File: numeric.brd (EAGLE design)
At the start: 94.9 x 61.6 mm, 28 parts, among them IC1 MEGA8-AI, Q2 BC817-16SMD, Q3 BC817-16SMD, SW2 EC12E_SW

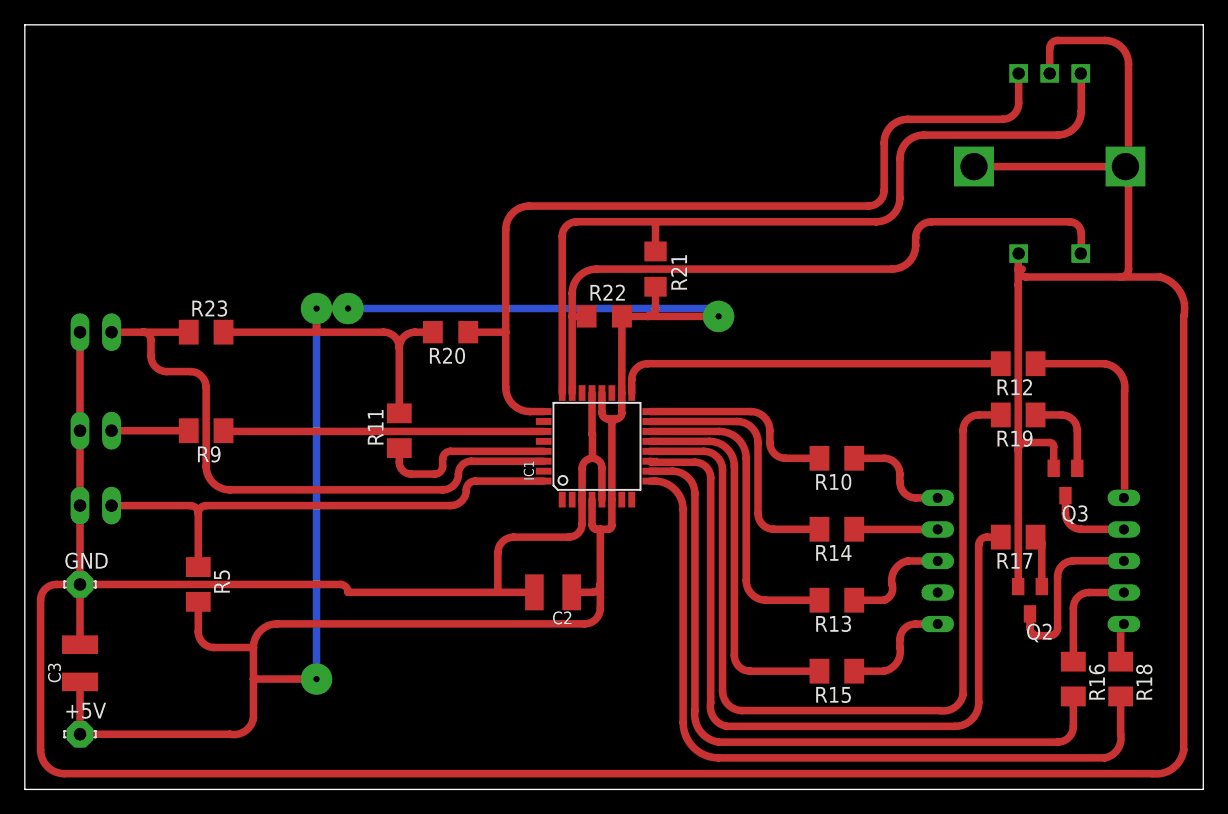
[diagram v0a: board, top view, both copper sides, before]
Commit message: Добавил разводку на горизонтальную плату
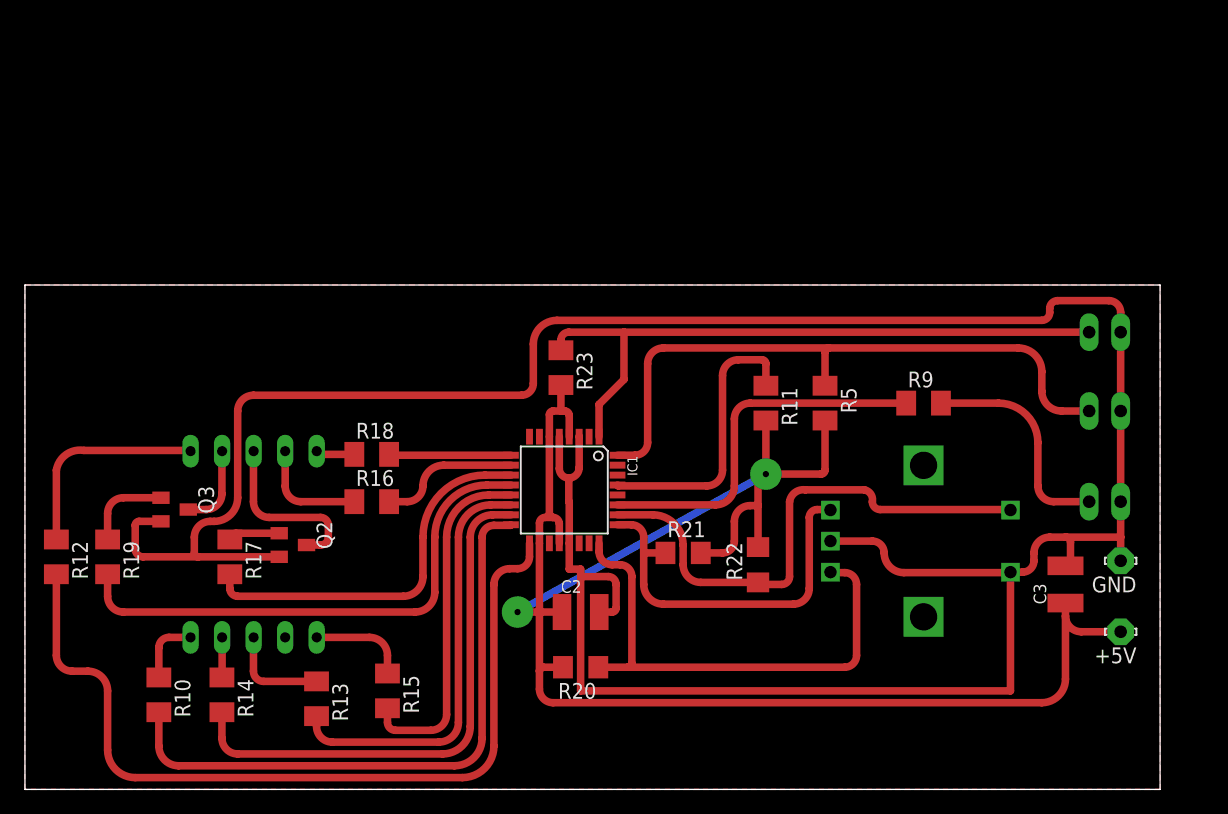
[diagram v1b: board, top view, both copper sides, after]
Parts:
- moved +5V 84.2 mm to (88.3, 12.7), turned to 180 degrees
- moved GND 83.8 mm to (88.3, 18.4), turned to 180 degrees
- moved TO_4N33 81.6 mm to (87.0, 30.5), turned to 0 degrees
- moved TO_MOC3061 81.5 mm to (87.0, 23.2), turned to 0 degrees
- moved BUTTON 81.3 mm to (87.0, 36.8), turned to 180 degrees
- moved C3 79.6 mm to (83.8, 16.5)
- moved R12 79.0 mm to (2.54, 18.7), turned to 270 degrees
- moved R19 74.2 mm to (6.67, 18.7), turned to 270 degrees
- moved Q3 71.8 mm to (12.1, 22.5), turned to 270 degrees
- moved DIS1 69.5 mm to (11.4, 19.4), turned to 0 degrees
- moved R17 63.5 mm to (16.5, 18.7), turned to 270 degrees
- moved R18 63.0 mm to (27.9, 27.0), turned to 0 degrees
- moved Q2 59.5 mm to (21.6, 19.7), turned to 270 degrees
- moved R16 58.3 mm to (27.9, 23.2), turned to 0 degrees
- moved R10 57.8 mm to (10.8, 7.62), turned to 270 degrees
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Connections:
- net N$1 renamed BASE_Q3
- net N$13 renamed RESET
- net N$2 renamed BASE_Q2
- net BUTT: now also IC1.1; no longer IC1.30
- net ENC_A: now also IC1.25; no longer IC1.24
- net ENC_B: now also IC1.24; no longer IC1.25
- net ENC_BUTT: now also IC1.26; no longer IC1.23
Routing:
- net GND: track 318.5 -> 231.5 mm
- net +5V: track 197.4 -> 140.7 mm, vias 4 -> 2
- net B1: track 61.2 -> 9.85 mm
- net B0: track 56.5 -> 11.0 mm
- net B6: track 31.3 -> 67.6 mm
- net ENC_A: track 65.9 -> 30.3 mm
- net B5: track 15.7 -> 49.3 mm
- net BASE_Q2: track 61.7 -> 30.0 mm
- net ENC_B: track 69.7 -> 41.0 mm
- net BASE_Q3: track 69.5 -> 41.6 mm
- net B4: track 20.6 -> 42.8 mm
- net ENC_BUTT: track 55.0 -> 42.3 mm
- net N$30: track 6.22 -> 17.3 mm
- net ZERODETECT: track 40.5 -> 51.5 mm
- net B3: track 25.0 -> 33.7 mm
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- added copper zone on layer 1, net GND
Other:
- board size 94.9 x 61.6 mm -> 91.4 x 40.6 mm

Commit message: Провел проверку DRC
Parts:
- C2, C3: device rcl:C1210K -> rcl:C1206K
- moved Q3 2.29 mm to (13.3, 24.4)
- moved Q2 2.29 mm to (22.9, 21.6)
- moved R16 2.29 mm to (29.2, 25.1)
- moved R17 2.29 mm to (17.8, 20.6)
- moved C3 1.80 mm to (85.1, 17.8)
- moved R23 1.80 mm to (44.5, 35.2)
- moved R20 1.80 mm to (46.0, 11.1)
- moved C2 1.80 mm to (46.0, 15.6)
- moved R11 1.80 mm to (61.0, 32.4)
- moved R22 1.80 mm to (60.3, 19.4)
- moved R10 1.80 mm to (12.1, 8.89)
- moved R12 1.80 mm to (3.81, 20.0)
- moved R14 1.80 mm to (17.1, 8.89)
- moved BUTTON 1.80 mm to (88.3, 38.1)
- moved DIS1 1.80 mm to (12.7, 20.6)
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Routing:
- net GND: track 231.5 -> 261.2 mm, vias 0 -> 2
- net BASE_Q3: track 41.6 -> 39.6 mm
- net N$21: track 14.4 -> 13.4 mm
- net N$19: track 8.90 -> 8.19 mm
- net N$23: track 6.92 -> 7.55 mm
- net BASE_Q2: track 30.0 -> 29.4 mm
- net N$22: track 6.68 -> 6.15 mm
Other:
- board size 91.4 x 40.6 mm -> 93.3 x 42.5 mm
